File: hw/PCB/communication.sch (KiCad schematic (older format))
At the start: 4 parts, among them J3 SMA, U4 RFM69HCW

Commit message: Specified the capacitance of the transceiver's capacitors. Updated the path of the library for the RFM69HCW.
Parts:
- Ca7: value C -> 0.1uF
- Cb7: value C -> 10uF
- U4: symbol RF_AM_FM:RFM69HCW -> RF_Module:RFM69HCW
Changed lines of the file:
@@
-EESchema Schematic File Version 4
+EESchema Schematic File Version 5
 LIBS:Femtosat-cache
 EELAYER 29 0
@@
 $EndDescr
 $Comp
-L RF_AM_FM:RFM69HCW U4
+L RF_Module:RFM69HCW U4
 U 1 1 5BD13EFB
 P 5600 3550
+AR Path="/5BD13EFB" Ref="U4"  Part="1"
+AR Path="/5BD13DD6/5BD13EFB" Ref="U4"  Part="1"
 F 0 "U4" H 5250 4000 50  0000 C CNN
 F 1 "RFM69HCW" H 5800 4000 50  0000 C CNN
@@
 P 6250 2850
 F 0 "Ca7" V 6150 2850 50  0000 C CNN
-F 1 "C" V 6250 2850 50  0000 C CNN
+F 1 "0.1uF" V 6250 2850 50  0000 C CNN
 F 2 "Capacitor_SMD:C_0603_1608Metric_Pad1.05x0.95mm_HandSolder" H 6288 2700 50  0001 C CNN
 F 3 "~" H 6250 2850 50  0001 C CNN
@@
 P 6250 3100
 F 0 "Cb7" V 6150 3100 50  0000 C CNN
-F 1 "C" V 6250 3100 50  0000 C CNN
+F 1 "10uF" V 6250 3100 50  0000 C CNN
 F 2 "Capacitor_SMD:C_0603_1608Metric_Pad1.05x0.95mm_HandSolder" H 6288 2950 50  0001 C CNN
 F 3 "~" H 6250 3100 50  0001 C CNN

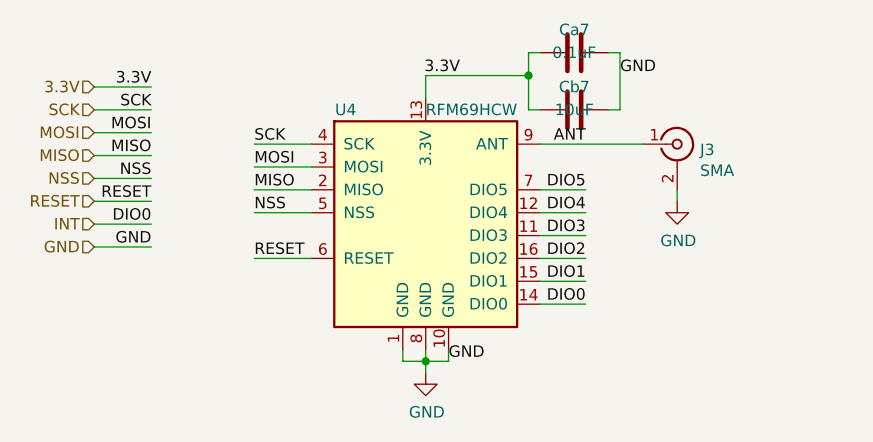
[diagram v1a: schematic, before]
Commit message: Added a footprint library for a micro SD card. Updated the schematic. Replaced the SAMD21G with the SAMD21E (32 pin variant). Added a data logger and a reset button.
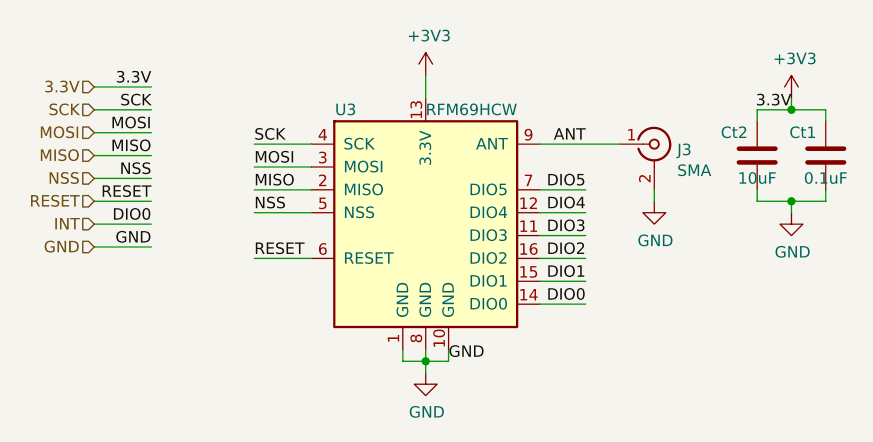
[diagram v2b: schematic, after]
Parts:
- renumbered Ca7 to Ct1, Cb7 to Ct2
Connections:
- net 3.3V renamed +3V3
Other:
- moved on the sheet: Ct1, Ct2, J3
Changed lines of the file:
@@
 $Descr A4 11693 8268
 encoding utf-8
-Sheet 4 5
+Sheet 4 6
 Title ""
 Date ""
@@
 P 5600 3550
 AR Path="/5BD13EFB" Ref="U4"  Part="1"
-AR Path="/5BD13DD6/5BD13EFB" Ref="U4"  Part="1"
-F 0 "U4" H 5250 4000 50  0000 C CNN
+AR Path="/5BD13DD6/5BD13EFB" Ref="U3"  Part="1"
+F 0 "U3" H 5250 4000 50  0000 C CNN
 F 1 "RFM69HCW" H 5800 4000 50  0000 C CNN
 F 2 "Transceptor:RFM69HCW" H 2300 5200 50  0001 C CNN
@@
 L antenna:SMA J3
 U 1 1 5BD153FD
-P 6700 3250
-F 0 "J3" H 6800 3225 50  0000 L CNN
-F 1 "SMA" H 6800 3134 50  0000 L CNN
-F 2 "Antenna:SMA" H 6700 3250 50  0001 C CNN
-F 3 "" H 6700 3250 50  0001 C CNN
-	1    6700 3250
+P 6600 3250
+F 0 "J3" H 6700 3225 50  0000 L CNN
+F 1 "SMA" H 6700 3134 50  0000 L CNN
+F 2 "Antenna:SMA" H 6600 3250 50  0001 C CNN
+F 3 "" H 6600 3250 50  0001 C CNN
+	1    6600 3250
 	1    0    0    -1
 $EndComp
@@
 	1    0    0    -1
 $EndComp
-Wire Wire Line
-	6550 3250 6100 3250
 Text Label 4850 3750 0    50   ~ 0
 RESET
@@
 Wire Wire Line
 	5600 3050 5600 2950
-Text Label 5750 2950 2    50   ~ 0
-3.3V
 Text HLabel 4150 3000 0    50   Input ~ 0
 3.3V
@@
 L power:GND #PWR0110
 U 1 1 5BD2EB6A
-P 6700 3500
-F 0 "#PWR0110" H 6700 3250 50  0001 C CNN
-F 1 "GND" H 6705 3327 50  0000 C CNN
-F 2 "" H 6700 3500 50  0001 C CNN
-F 3 "" H 6700 3500 50  0001 C CNN
-	1    6700 3500
-	1    0    0    -1
-$EndComp
-Wire Wire Line
-	6700 3450 6700 3500
-$Comp
-L Device:C Ca7
+P 6600 3500
+F 0 "#PWR0110" H 6600 3250 50  0001 C CNN
+F 1 "GND" H 6605 3327 50  0000 C CNN
+F 2 "" H 6600 3500 50  0001 C CNN
+F 3 "" H 6600 3500 50  0001 C CNN
+	1    6600 3500
+	1    0    0    -1
+$EndComp
+Wire Wire Line
+	6600 3450 6600 3500
+$Comp
+L Device:C Ct1
 U 1 1 5BD8FE47
-P 6250 2850
-F 0 "Ca7" V 6150 2850 50  0000 C CNN
-F 1 "0.1uF" V 6250 2850 50  0000 C CNN
-F 2 "Capacitor_SMD:C_0603_1608Metric_Pad1.05x0.95mm_HandSolder" H 6288 2700 50  0001 C CNN
-F 3 "~" H 6250 2850 50  0001 C CNN
-	1    6250 2850
-	0    1    1    0
-$EndComp
-$Comp
-L Device:C Cb7
+P 7350 3300
+F 0 "Ct1" H 7450 3200 50  0000 C CNN
+F 1 "0.1uF" H 7350 3400 50  0000 C CNN
+F 2 "Capacitor_SMD:C_0603_1608Metric_Pad1.05x0.95mm_HandSolder" H 7388 3150 50  0001 C CNN
+F 3 "~" H 7350 3300 50  0001 C CNN
+	1    7350 3300
+	-1   0    0    1
+$EndComp
+$Comp
+L Device:C Ct2
 U 1 1 5BD90136
-P 6250 3100
-F 0 "Cb7" V 6150 3100 50  0000 C CNN
-F 1 "10uF" V 6250 3100 50  0000 C CNN
-F 2 "Capacitor_SMD:C_0603_1608Metric_Pad1.05x0.95mm_HandSolder" H 6288 2950 50  0001 C CNN
-F 3 "~" H 6250 3100 50  0001 C CNN
-	1    6250 3100
-	0    1    1    0
-$EndComp
-Wire Wire Line
-	6100 2850 6050 2850
-Wire Wire Line
-	6050 2850 6050 2950
-Wire Wire Line
-	6050 3100 6100 3100
-Wire Wire Line
-	5600 2950 6050 2950
-Connection ~ 6050 2950
-Wire Wire Line
-	6050 2950 6050 3100
-Wire Wire Line
-	6400 2850 6450 2850
-Wire Wire Line
-	6450 2850 6450 3100
-Wire Wire Line
-	6450 3100 6400 3100
-Text Label 6450 2950 0    50   ~ 0
-GND
+P 7050 3300
+F 0 "Ct2" H 7150 3200 50  0000 C CNN
+F 1 "10uF" H 7050 3400 50  0000 C CNN
+F 2 "Capacitor_SMD:C_0603_1608Metric_Pad1.05x0.95mm_HandSolder" H 7088 3150 50  0001 C CNN
+F 3 "~" H 7050 3300 50  0001 C CNN
+	1    7050 3300
+	-1   0    0    1
+$EndComp
+Wire Wire Line
+	7350 3150 7350 3100
+Wire Wire Line
+	7050 3100 7050 3150
+Wire Wire Line
+	7350 3450 7350 3500
+Wire Wire Line
+	7050 3500 7050 3450
 Text Label 6300 3250 2    50   ~ 0
 ANT
+$Comp
+L power:+3V3 #PWR?
+U 1 1 5D1D8537
+P 5600 2950
+F 0 "#PWR?" H 5600 2800 50  0001 C CNN
+F 1 "+3V3" H 5615 3123 50  0000 C CNN
+F 2 "" H 5600 2950 50  0001 C CNN
+F 3 "" H 5600 2950 50  0001 C CNN
+	1    5600 2950
+	1    0    0    -1
+$EndComp
+$Comp
+L power:+3V3 #PWR?
+U 1 1 5D1D89F4
+P 7200 3050
+F 0 "#PWR?" H 7200 2900 50  0001 C CNN
+F 1 "+3V3" H 7215 3223 50  0000 C CNN
+F 2 "" H 7200 3050 50  0001 C CNN
+F 3 "" H 7200 3050 50  0001 C CNN
+	1    7200 3050
+	1    0    0    -1
+$EndComp
+$Comp
+L power:GND #PWR?
+U 1 1 5D1D8ED6
+P 7200 3550
+F 0 "#PWR?" H 7200 3300 50  0001 C CNN
+F 1 "GND" H 7205 3377 50  0000 C CNN
+F 2 "" H 7200 3550 50  0001 C CNN
+F 3 "" H 7200 3550 50  0001 C CNN
+	1    7200 3550
+	1    0    0    -1
+$EndComp
+Wire Wire Line
+	7050 3100 7200 3100
+Wire Wire Line
+	7050 3500 7200 3500
+Wire Wire Line
+	7200 3550 7200 3500
+Connection ~ 7200 3500
+Wire Wire Line
+	7200 3500 7350 3500
+Wire Wire Line
+	7200 3100 7200 3050
+Connection ~ 7200 3100
+Wire Wire Line
+	7200 3100 7350 3100
+Wire Wire Line
+	6100 3250 6450 3250
+Text Label 7200 3100 2    50   ~ 0
+3.3V
 $EndSCHEMATC

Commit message: Final revision check. Generated the Gerber files.
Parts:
- removed J3: SMA, Antenna:SMA, symbol antenna:SMA
- added J3: U.FL, Connector_Coaxial:U.FL_Hirose_U.FL-R-SMT-1_Vertical, symbol Connector:Conn_Coaxial
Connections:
- net ANT: now also J3.1 (In)
- net GND: now also J3.2 (Ext)
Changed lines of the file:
@@
-	1    0    0    -1
-$EndComp
-$Comp
-L antenna:SMA J3
-U 1 1 5BD153FD
-P 6600 3250
-F 0 "J3" H 6700 3225 50  0000 L CNN
-F 1 "SMA" H 6700 3134 50  0000 L CNN
-F 2 "Antenna:SMA" H 6600 3250 50  0001 C CNN
-F 3 "" H 6600 3250 50  0001 C CNN
-	1    6600 3250
 	1    0    0    -1
 $EndComp
@@
 Wire Wire Line
 	7200 3100 7350 3100
-Wire Wire Line
-	6100 3250 6450 3250
 Text Label 7200 3100 2    50   ~ 0
 3.3V
+$Comp
+L Connector:Conn_Coaxial J3
+U 1 1 5D24BE5C
+P 6600 3250
+F 0 "J3" H 6700 3225 50  0000 L CNN
+F 1 "U.FL" H 6700 3134 50  0000 L CNN
+F 2 "Connector_Coaxial:U.FL_Hirose_U.FL-R-SMT-1_Vertical" H 6600 3250 50  0001 C CNN
+F 3 " ~" H 6600 3250 50  0001 C CNN
+	1    6600 3250
+	1    0    0    -1
+$EndComp
+Wire Wire Line
+	6100 3250 6400 3250
 $EndSCHEMATC
